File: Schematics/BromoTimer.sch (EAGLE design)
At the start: 23 parts, among them IC1 PIC16F687, IC2 7805TV, K1 351, K2 351, Q1 2N3565, Q2 2N3565, X4 22-23-2021

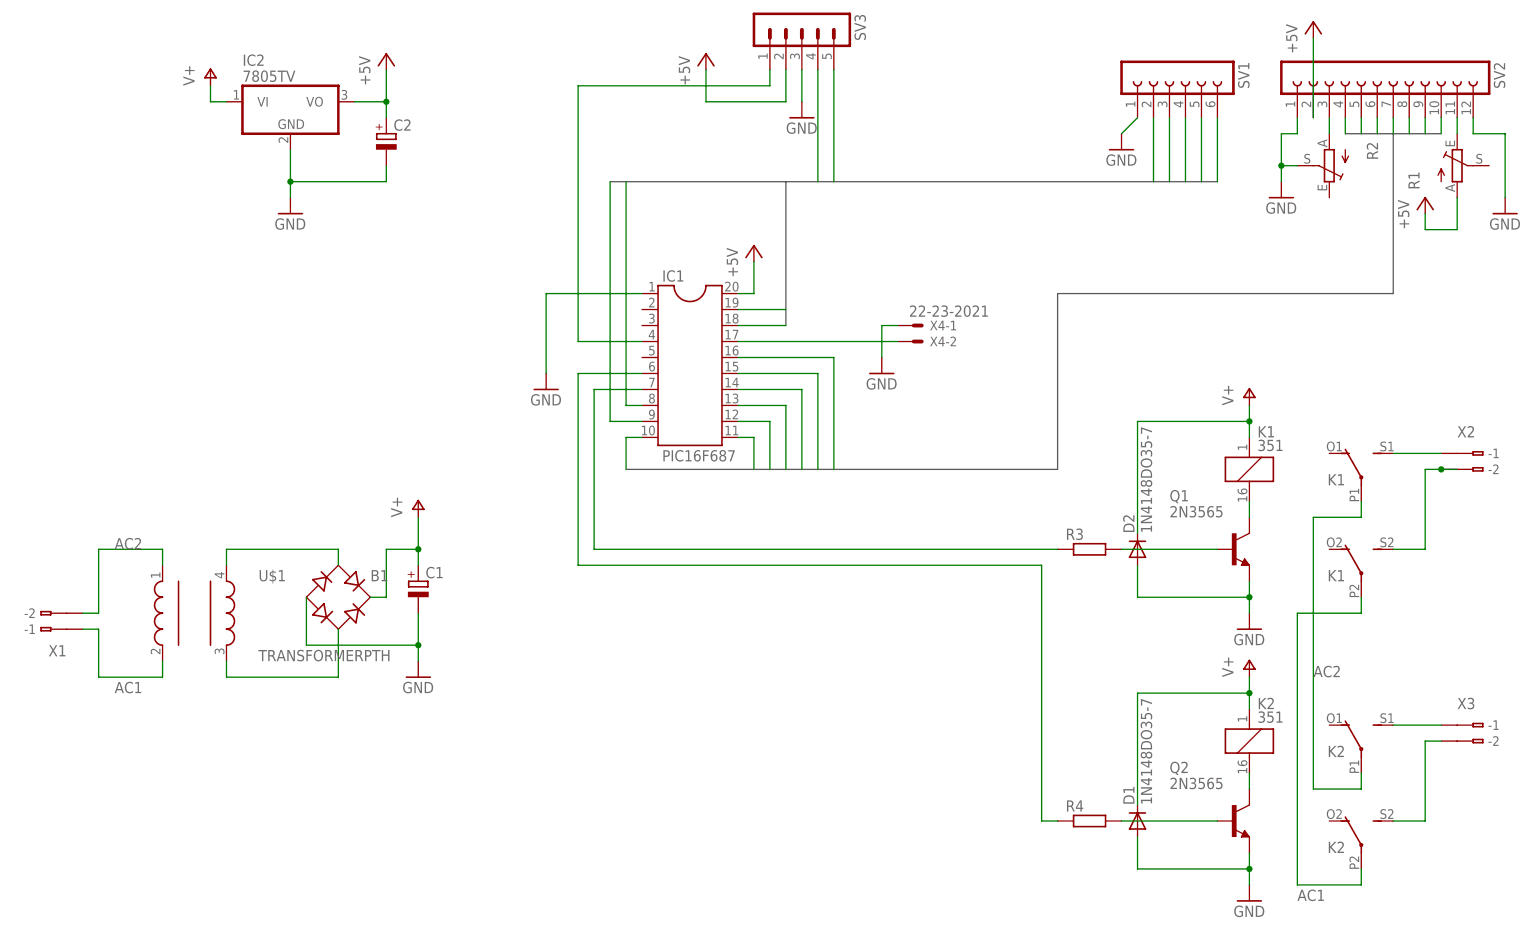
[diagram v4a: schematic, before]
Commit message: Add buzzer and diode protection to 7805.
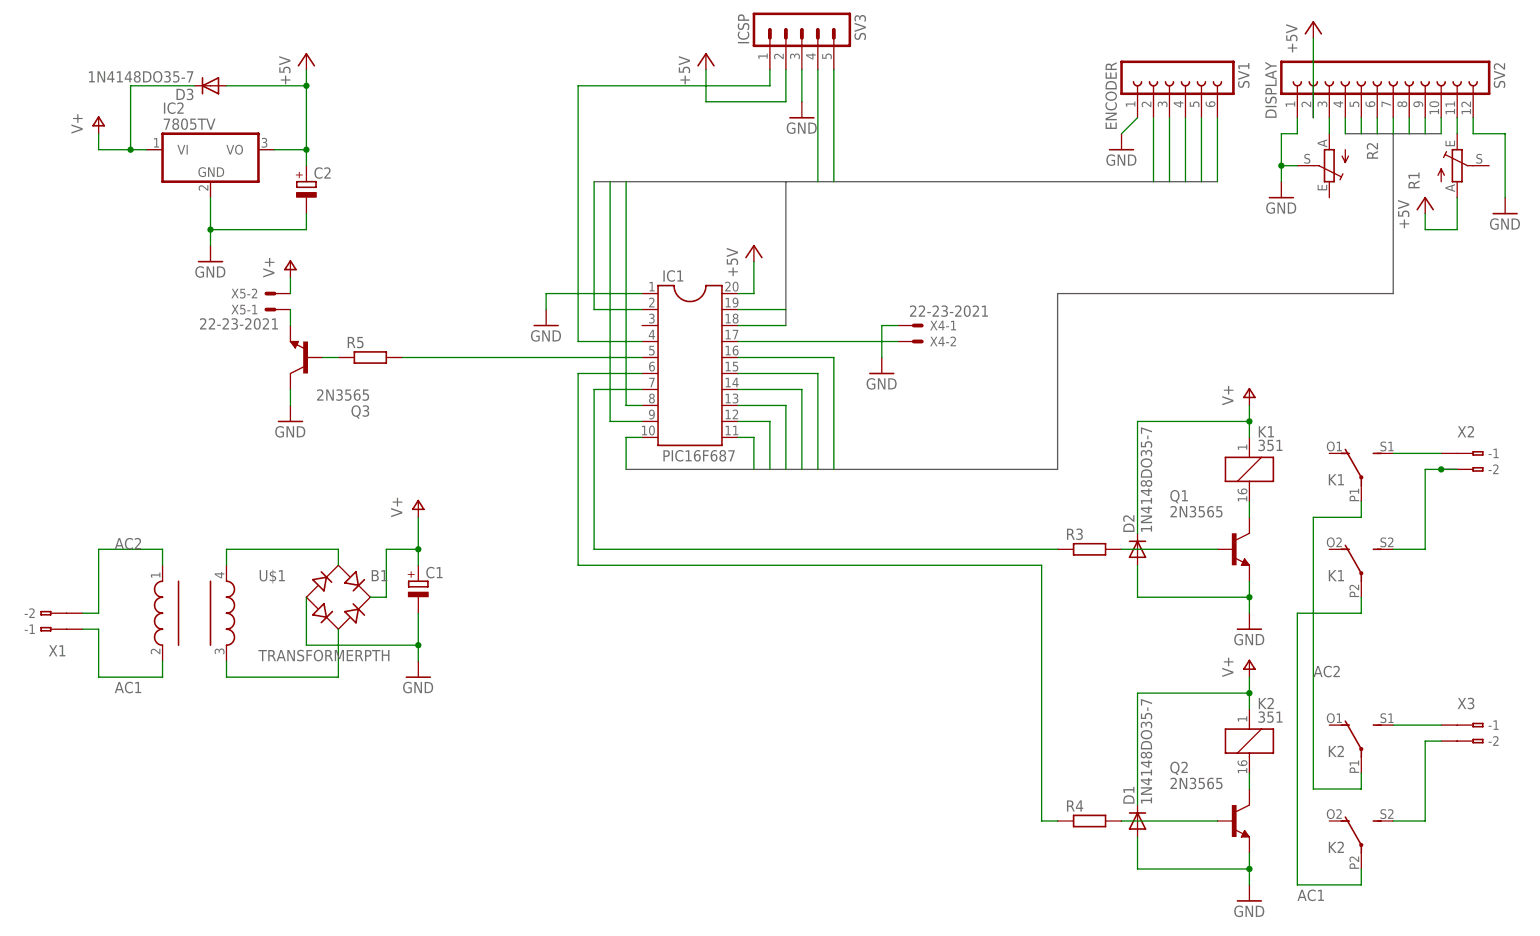
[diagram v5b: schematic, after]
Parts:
- added D3: 1N4148DO35-7, diode:1N4148DO35-7
- added Q3: 2N3565, transistor-npn:2N3565
- added R5: (no value), rcl:R-EU_0207/10
- added X5: 22-23-2021, con-molex:22-23-2021
- SV1: value (none) -> ENCODER
- SV2: value (none) -> DISPLAY
- SV3: value (none) -> ICSP
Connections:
- new net N$17: IC1.5, R5.2
- new net N$18: Q3.B, R5.1
- new net N$19: Q3.E, X5-1.S
- net +5V: now also D3.A
- net GND: now also Q3.C
- net SW: now also IC1.2
- net V+: now also D3.C, X5-2.S
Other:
- moved on the sheet: C2, IC2
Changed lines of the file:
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@@
 <part name="IC1" library="ic-package" deviceset="DIL20" device="S" value="PIC16F687"/>
 <part name="FRAME1" library="frames" deviceset="A4L-LOC" device=""/>
-<part name="SV1" library="con-lsta" deviceset="FE06-1" device=""/>
-<part name="SV2" library="con-lsta" deviceset="FE12-1" device=""/>
+<part name="SV1" library="con-lsta" deviceset="FE06-1" device="" value="ENCODER"/>
+<part name="SV2" library="con-lsta" deviceset="FE12-1" device="" value="DISPLAY"/>
 <part name="IC2" library="linear" deviceset="78*" device="TV" technology="05"/>
 <part name="P+1" library="supply1" deviceset="+5V" device=""/>
@@
 <part name="D1" library="diode" deviceset="1N4148" device="DO35-7"/>
 <part name="D2" library="diode" deviceset="1N4148" device="DO35-7"/>
-<part name="SV3" library="con-lstb" deviceset="MA05-1" device=""/>
+<part name="SV3" library="con-lstb" deviceset="MA05-1" device="" value="ICSP"/>
 <part name="P+9" library="supply1" deviceset="+5V" device=""/>
 <part name="GND10" library="supply1" deviceset="GND" device=""/>
+<part name="D3" library="diode" deviceset="1N4148" device="DO35-7"/>
+<part name="Q3" library="transistor-npn" deviceset="2N3565" device=""/>
+<part name="R5" library="rcl" deviceset="R-EU_" device="0207/10"/>
+<part name="GND11" library="supply1" deviceset="GND" device=""/>
+<part name="X5" library="con-molex" deviceset="22-23-2021" device=""/>
+<part name="P+10" library="supply1" deviceset="V+" device=""/>
 </parts>
 <sheets>
@@
 <instance part="SV1" gate="G$1" x="193.04" y="162.56" rot="R270"/>
 <instance part="SV2" gate="G$1" x="226.06" y="162.56" rot="R270"/>
-<instance part="IC2" gate="A1" x="53.34" y="157.48"/>
-<instance part="P+1" gate="1" x="68.58" y="165.1"/>
-<instance part="GND1" gate="1" x="53.34" y="139.7"/>
+<instance part="IC2" gate="A1" x="40.64" y="149.86"/>
+<instance part="P+1" gate="1" x="55.88" y="165.1"/>
+<instance part="GND1" gate="1" x="40.64" y="132.08"/>
 <instance part="C1" gate="G$1" x="73.66" y="81.28"/>
-<instance part="C2" gate="G$1" x="68.58" y="152.4"/>
-<instance part="GND2" gate="1" x="93.98" y="111.76"/>
+<instance part="C2" gate="G$1" x="55.88" y="144.78"/>
+<instance part="GND2" gate="1" x="93.98" y="121.92"/>
 <instance part="P+2" gate="1" x="127" y="134.62"/>
 <instance part="GND3" gate="1" x="210.82" y="142.24"/>
@@
 <instance part="P+7" gate="1" x="73.66" y="93.98"/>
 <instance part="GND7" gate="1" x="73.66" y="66.04"/>
-<instance part="P+8" gate="1" x="40.64" y="162.56"/>
+<instance part="P+8" gate="1" x="22.86" y="154.94"/>
 <instance part="X4" gate="-1" x="152.4" y="121.92"/>
 <instance part="X4" gate="-2" x="152.4" y="119.38"/>
@@
 <instance part="P+9" gate="1" x="119.38" y="165.1"/>
 <instance part="GND10" gate="1" x="134.62" y="154.94"/>
+<instance part="D3" gate="G$1" x="40.64" y="160.02" rot="R180"/>
+<instance part="Q3" gate="G$1" x="55.88" y="116.84" rot="R180"/>
+<instance part="R5" gate="G$1" x="66.04" y="116.84"/>
+<instance part="GND11" gate="1" x="53.34" y="106.68"/>
+<instance part="X5" gate="-1" x="50.8" y="124.46" rot="R180"/>
+<instance part="X5" gate="-2" x="50.8" y="127" rot="R180"/>
+<instance part="P+10" gate="1" x="53.34" y="132.08"/>
 </instances>
 <busses>
@@
 <wire x1="200.66" y1="144.78" x2="132.08" y2="144.78" width="0.762" layer="92"/>
 <wire x1="132.08" y1="144.78" x2="132.08" y2="121.92" width="0.762" layer="92"/>
-<wire x1="132.08" y1="144.78" x2="104.14" y2="144.78" width="0.762" layer="92"/>
+<wire x1="132.08" y1="144.78" x2="101.6" y2="144.78" width="0.762" layer="92"/>
 </segment>
 </bus>
@@
 <nets>
 <net name="+5V" class="0">
-<segment>
-<pinref part="IC2" gate="A1" pin="VO"/>
-<pinref part="P+1" gate="1" pin="+5V"/>
-<wire x1="63.5" y1="157.48" x2="68.58" y2="157.48" width="0.1524" layer="91"/>
-<wire x1="68.58" y1="157.48" x2="68.58" y2="162.56" width="0.1524" layer="91"/>
-<pinref part="C2" gate="G$1" pin="+"/>
-<wire x1="68.58" y1="154.94" x2="68.58" y2="157.48" width="0.1524" layer="91"/>
-<junction x="68.58" y="157.48"/>
-</segment>
 <segment>
 <pinref part="P+2" gate="1" pin="+5V"/>
@@
 <pinref part="P+9" gate="1" pin="+5V"/>
 </segment>
+<segment>
+<pinref part="IC2" gate="A1" pin="VO"/>
+<wire x1="50.8" y1="149.86" x2="55.88" y2="149.86" width="0.1524" layer="91"/>
+<pinref part="C2" gate="G$1" pin="+"/>
+<wire x1="55.88" y1="147.32" x2="55.88" y2="149.86" width="0.1524" layer="91"/>
+<pinref part="D3" gate="G$1" pin="A"/>
+<wire x1="43.18" y1="160.02" x2="55.88" y2="160.02" width="0.1524" layer="91"/>
+<wire x1="55.88" y1="160.02" x2="55.88" y2="149.86" width="0.1524" layer="91"/>
+<junction x="55.88" y="149.86"/>
+<pinref part="P+1" gate="1" pin="+5V"/>
+<wire x1="55.88" y1="162.56" x2="55.88" y2="160.02" width="0.1524" layer="91"/>
+<junction x="55.88" y="160.02"/>
+</segment>
 </net>
 <net name="GND" class="0">
@@
 <pinref part="IC2" gate="A1" pin="GND"/>
 <pinref part="GND1" gate="1" pin="GND"/>
-<wire x1="53.34" y1="149.86" x2="53.34" y2="144.78" width="0.1524" layer="91"/>
-<wire x1="53.34" y1="144.78" x2="53.34" y2="142.24" width="0.1524" layer="91"/>
-<junction x="53.34" y="144.78"/>
+<wire x1="40.64" y1="142.24" x2="40.64" y2="137.16" width="0.1524" layer="91"/>
+<wire x1="40.64" y1="137.16" x2="40.64" y2="134.62" width="0.1524" layer="91"/>
+<junction x="40.64" y="137.16"/>
 <pinref part="C2" gate="G$1" pin="-"/>
-<wire x1="68.58" y1="147.32" x2="68.58" y2="144.78" width="0.1524" layer="91"/>
-<wire x1="68.58" y1="144.78" x2="53.34" y2="144.78" width="0.1524" layer="91"/>
+<wire x1="55.88" y1="139.7" x2="55.88" y2="137.16" width="0.1524" layer="91"/>
+<wire x1="55.88" y1="137.16" x2="40.64" y2="137.16" width="0.1524" layer="91"/>
 </segment>
 <segment>
@@
 <pinref part="GND2" gate="1" pin="GND"/>
 <wire x1="109.22" y1="127" x2="93.98" y2="127" width="0.1524" layer="91"/>
-<wire x1="93.98" y1="127" x2="93.98" y2="114.3" width="0.1524" layer="91"/>
+<wire x1="93.98" y1="127" x2="93.98" y2="124.46" width="0.1524" layer="91"/>
 </segment>
 <segment>
@@
 <wire x1="134.62" y1="162.56" x2="134.62" y2="157.48" width="0.1524" layer="91"/>
 </segment>
+<segment>
+<pinref part="Q3" gate="G$1" pin="C"/>
+<pinref part="GND11" gate="1" pin="GND"/>
+<wire x1="53.34" y1="111.76" x2="53.34" y2="109.22" width="0.1524" layer="91"/>
+</segment>
 </net>
 <net name="RS" class="0">
@@
 <pinref part="SV1" gate="G$1" pin="4"/>
 <wire x1="195.58" y1="154.94" x2="195.58" y2="144.78" width="0.1524" layer="91"/>
+</segment>
+<segment>
+<pinref part="IC1" gate="G$1" pin="2"/>
+<wire x1="109.22" y1="124.46" x2="101.6" y2="124.46" width="0.1524" layer="91"/>
+<wire x1="101.6" y1="124.46" x2="101.6" y2="144.78" width="0.1524" layer="91"/>
 </segment>
 </net>
@@
 <segment>
 <pinref part="P+8" gate="1" pin="V+"/>
-<wire x1="40.64" y1="160.02" x2="40.64" y2="157.48" width="0.1524" layer="91"/>
+<wire x1="22.86" y1="152.4" x2="22.86" y2="149.86" width="0.1524" layer="91"/>
 <pinref part="IC2" gate="A1" pin="VI"/>
-<wire x1="40.64" y1="157.48" x2="43.18" y2="157.48" width="0.1524" layer="91"/>
+<wire x1="22.86" y1="149.86" x2="27.94" y2="149.86" width="0.1524" layer="91"/>
+<pinref part="D3" gate="G$1" pin="C"/>
+<wire x1="27.94" y1="149.86" x2="30.48" y2="149.86" width="0.1524" layer="91"/>
+<wire x1="38.1" y1="160.02" x2="27.94" y2="160.02" width="0.1524" layer="91"/>
+<wire x1="27.94" y1="160.02" x2="27.94" y2="149.86" width="0.1524" layer="91"/>
+<junction x="27.94" y="149.86"/>
 </segment>
 <segment>
@@
 <junction x="205.74" y="106.68"/>
 </segment>
+<segment>
+<pinref part="P+10" gate="1" pin="V+"/>
+<pinref part="X5" gate="-2" pin="S"/>
+<wire x1="53.34" y1="129.54" x2="53.34" y2="127" width="0.1524" layer="91"/>
+</segment>
 </net>
 <net name="N$13" class="0">
@@
 </segment>
 </net>
+<net name="N$17" class="0">
+<segment>
+<pinref part="R5" gate="G$1" pin="2"/>
+<pinref part="IC1" gate="G$1" pin="5"/>
+<wire x1="71.12" y1="116.84" x2="109.22" y2="116.84" width="0.1524" layer="91"/>
+</segment>
+</net>
+<net name="N$18" class="0">
+<segment>
+<pinref part="R5" gate="G$1" pin="1"/>
+<pinref part="Q3" gate="G$1" pin="B"/>
+<wire x1="60.96" y1="116.84" x2="58.42" y2="116.84" width="0.1524" layer="91"/>
+</segment>
+</net>
+<net name="N$19" class="0">
+<segment>
+<pinref part="Q3" gate="G$1" pin="E"/>
+<pinref part="X5" gate="-1" pin="S"/>
+<wire x1="53.34" y1="124.46" x2="53.34" y2="121.92" width="0.1524" layer="91"/>
+</segment>
+</net>
